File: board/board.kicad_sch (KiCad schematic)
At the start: 4 parts, among them J1 019_100BASE-T_with_CT, J2 009_1000BASE-T, J3 004_BASE-T_CT

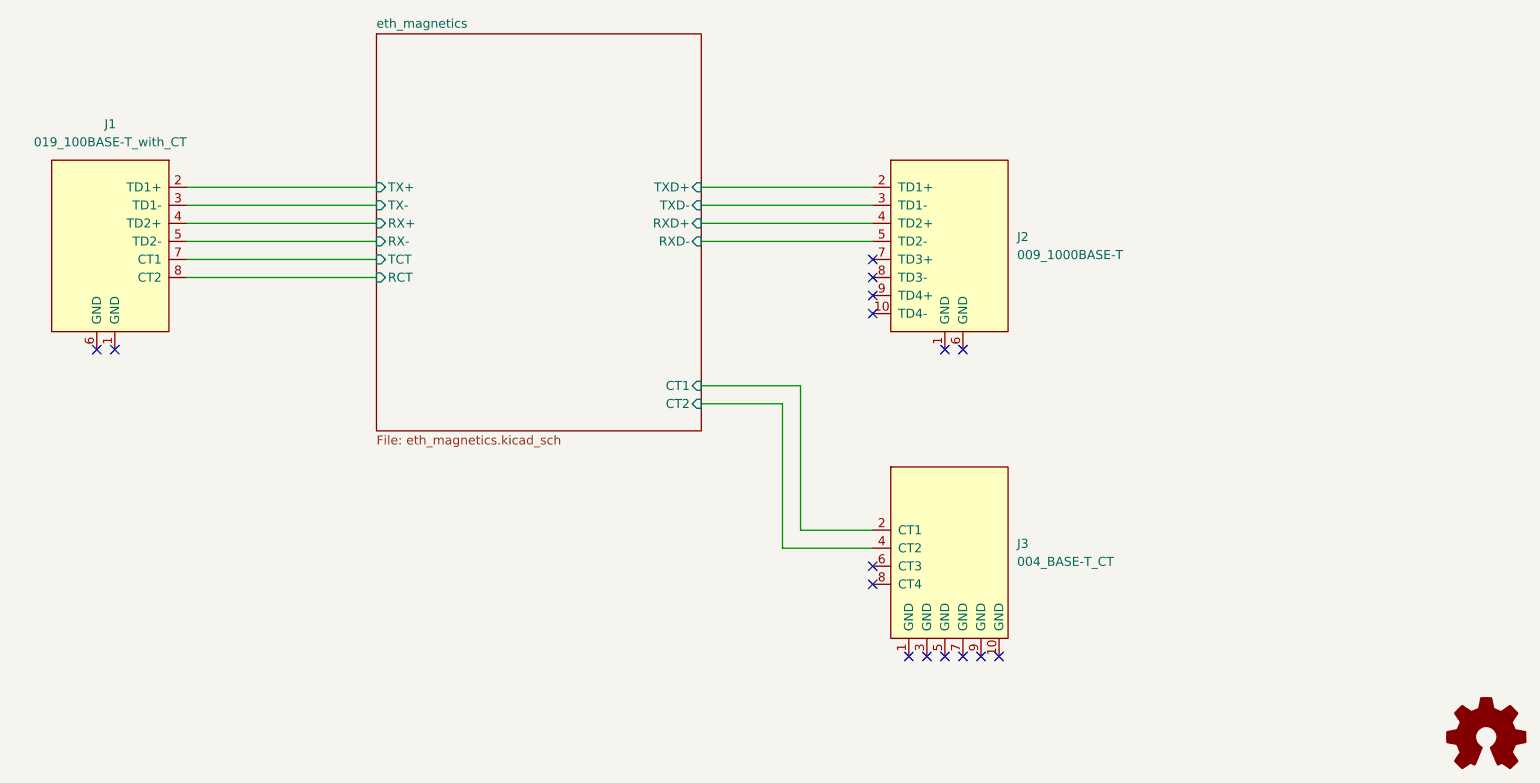
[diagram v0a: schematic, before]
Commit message: updated to use put_on_edge v1.0 connectors
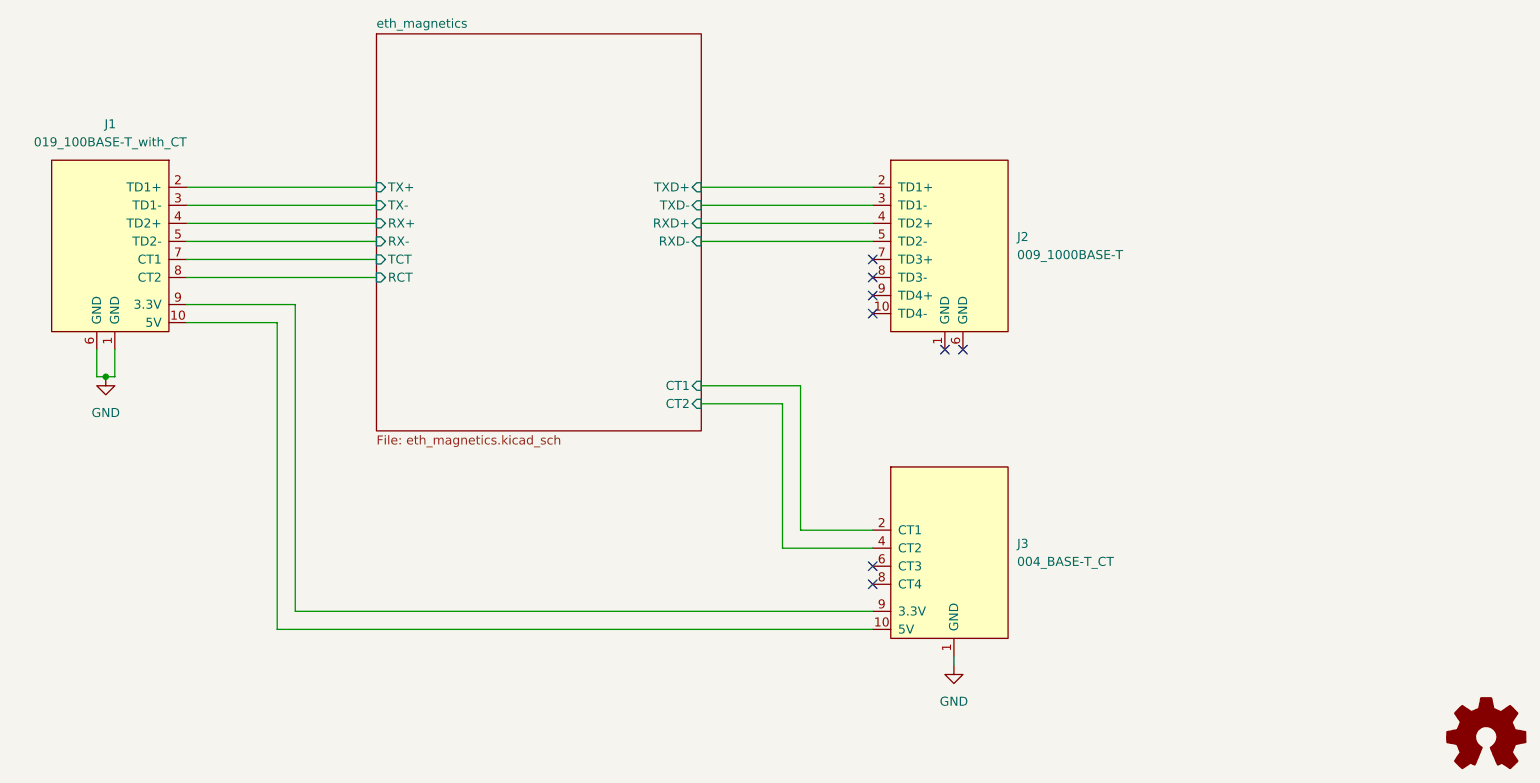
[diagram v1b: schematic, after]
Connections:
- net GND: now reaches J3.1 (GND)
- net GND: now also J1.1 (GND), J1.6 (GND)
- net at J3.10 (5V): now also J1.10 (5V)
- net at J3.9 (3.3V): now also J1.9 (3.3V)
- no-connect marks 16 -> 8
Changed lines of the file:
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@@
 (kicad_sch (version 20211123) (generator eeschema)
   (paper "A4")
-  (no_connect (at 80.01 102.87))
-  (no_connect (at 77.47 102.87))
+  (junction (at 78.74 106.68) (diameter 0) (color 0 0 0 0)
+  )
   (no_connect (at 186.69 90.17))
   (no_connect (at 186.69 95.25))
   (no_connect (at 186.69 92.71))
   (no_connect (at 186.69 97.79))
-  (no_connect (at 204.47 146.05))
-  (no_connect (at 194.31 146.05))
-  (no_connect (at 196.85 146.05))
-  (no_connect (at 199.39 146.05))
-  (no_connect (at 201.93 146.05))
   (no_connect (at 199.39 102.87))
   (no_connect (at 196.85 102.87))
-  (no_connect (at 191.77 146.05))
   (no_connect (at 186.69 135.89))
   (no_connect (at 186.69 133.35))
@@
     (stroke (width 0) (type default) (color 0 0 0 0))
   )
+  (wire (pts (xy 186.69 139.7) (xy 105.41 139.7))
+    (stroke (width 0) (type default) (color 0 0 0 0))
+  )
+  (wire (pts (xy 80.01 106.68) (xy 80.01 102.87))
+    (stroke (width 0) (type default) (color 0 0 0 0))
+  )
   (wire (pts (xy 90.17 82.55) (xy 116.84 82.55))
     (stroke (width 0) (type default) (color 0 0 0 0))
   )
+  (wire (pts (xy 77.47 102.87) (xy 77.47 106.68))
+    (stroke (width 0) (type default) (color 0 0 0 0))
+  )
   (wire (pts (xy 162.56 85.09) (xy 186.69 85.09))
     (stroke (width 0) (type default) (color 0 0 0 0))
@@
     (stroke (width 0) (type default) (color 0 0 0 0))
   )
+  (wire (pts (xy 77.47 106.68) (xy 78.74 106.68))
+    (stroke (width 0) (type default) (color 0 0 0 0))
+  )
   (wire (pts (xy 162.56 107.95) (xy 176.53 107.95))
     (stroke (width 0) (type default) (color 0 0 0 0))
   )
+  (wire (pts (xy 78.74 106.68) (xy 80.01 106.68))
+    (stroke (width 0) (type default) (color 0 0 0 0))
+  )
+  (wire (pts (xy 105.41 139.7) (xy 105.41 96.52))
+    (stroke (width 0) (type default) (color 0 0 0 0))
+  )
   (wire (pts (xy 176.53 128.27) (xy 186.69 128.27))
     (stroke (width 0) (type default) (color 0 0 0 0))
@@
     (stroke (width 0) (type default) (color 0 0 0 0))
   )
+  (wire (pts (xy 198.12 146.05) (xy 198.12 147.32))
+    (stroke (width 0) (type default) (color 0 0 0 0))
+  )
+  (wire (pts (xy 105.41 96.52) (xy 90.17 96.52))
+    (stroke (width 0) (type default) (color 0 0 0 0))
+  )
   (wire (pts (xy 173.99 110.49) (xy 173.99 130.81))
     (stroke (width 0) (type default) (color 0 0 0 0))
@@
     (stroke (width 0) (type default) (color 0 0 0 0))
   )
+  (wire (pts (xy 102.87 99.06) (xy 102.87 142.24))
+    (stroke (width 0) (type default) (color 0 0 0 0))
+  )
   (wire (pts (xy 90.17 85.09) (xy 116.84 85.09))
     (stroke (width 0) (type default) (color 0 0 0 0))
@@
     (stroke (width 0) (type default) (color 0 0 0 0))
   )
+  (wire (pts (xy 90.17 99.06) (xy 102.87 99.06))
+    (stroke (width 0) (type default) (color 0 0 0 0))
+  )
+  (wire (pts (xy 102.87 142.24) (xy 186.69 142.24))
+    (stroke (width 0) (type default) (color 0 0 0 0))
+  )
+  (symbol (lib_id "power:GND") (at 198.12 147.32 0) (unit 1)
+    (in_bom yes) (on_board yes) (fields_autoplaced)
+    (property "Reference" "#PWR0102" (id 0) (at 198.12 153.67 0)
+      (effects (font (size 1.27 1.27)) hide)
+    )
+    (property "Value" "GND" (id 1) (at 198.12 152.4 0))
+    (property "Footprint" "" (id 2) (at 198.12 147.32 0)
+      (effects (font (size 1.27 1.27)) hide)
+    )
+    (property "Datasheet" "" (id 3) (at 198.12 147.32 0)
+      (effects (font (size 1.27 1.27)) hide)
+    )
+    (pin "1")
+  )
   (symbol (lib_id "Graphic:Logo_Open_Hardware_Small") (at 273.05 157.48 0) (unit 1)
     (in_bom yes) (on_board yes) (fields_autoplaced)
@@
     )
     (property "Datasheet" "" (id 3) (at 205.74 115.57 0)
+      (effects (font (size 1.27 1.27)) hide)
+    )
+    (pin "1")
+    (pin "10")
+    (pin "2")
+    (pin "4")
+    (pin "6")
+    (pin "8")
+    (pin "9")
+  )
+  (symbol (lib_id "put_on_edge:019_100BASE-T_with_CT") (at 78.74 88.9 0) (mirror y) (unit 1)
+    (in_bom yes) (on_board yes) (fields_autoplaced)
+    (property "Reference" "J1" (id 0) (at 79.375 71.12 0))
+    (property "Value" "019_100BASE-T_with_CT" (id 1) (at 79.375 73.66 0))
+    (property "Footprint" "on_edge:on_edge_2x05_device" (id 2) (at 71.12 72.39 0)
+      (effects (font (size 1.27 1.27)) hide)
+    )
+    (property "Datasheet" "" (id 3) (at 71.12 72.39 0)
       (effects (font (size 1.27 1.27)) hide)
     )
@@
     (pin "9")
   )
-  (symbol (lib_id "put_on_edge:019_100BASE-T_with_CT") (at 78.74 88.9 0) (mirror y) (unit 1)
-    (in_bom yes) (on_board yes) (fields_autoplaced)
-    (property "Reference" "J1" (id 0) (at 79.375 71.12 0))
-    (property "Value" "019_100BASE-T_with_CT" (id 1) (at 79.375 73.66 0))
-    (property "Footprint" "on_edge:on_edge_2x05_device" (id 2) (at 71.12 72.39 0)
-      (effects (font (size 1.27 1.27)) hide)
-    )
-    (property "Datasheet" "" (id 3) (at 71.12 72.39 0)
-      (effects (font (size 1.27 1.27)) hide)
-    )
-    (pin "1")
-    (pin "2")
-    (pin "3")
-    (pin "4")
-    (pin "5")
-    (pin "6")
-    (pin "7")
-    (pin "8")
-  )
   (symbol (lib_id "put_on_edge:009_1000BASE-T") (at 198.12 88.9 0) (unit 1)
     (in_bom yes) (on_board yes) (fields_autoplaced)
@@
     (pin "9")
   )
+  (symbol (lib_id "power:GND") (at 78.74 106.68 0) (unit 1)
+    (in_bom yes) (on_board yes) (fields_autoplaced)
+    (property "Reference" "#PWR0101" (id 0) (at 78.74 113.03 0)
+      (effects (font (size 1.27 1.27)) hide)
+    )
+    (property "Value" "GND" (id 1) (at 78.74 111.76 0))
+    (property "Footprint" "" (id 2) (at 78.74 106.68 0)
+      (effects (font (size 1.27 1.27)) hide)
+    )
+    (property "Datasheet" "" (id 3) (at 78.74 106.68 0)
+      (effects (font (size 1.27 1.27)) hide)
+    )
+    (pin "1")
+  )
   (sheet (at 116.84 58.42) (size 45.72 55.88) (fields_autoplaced)
     (stroke (width 0.1524) (type solid) (color 0 0 0 0))
@@
   )
   (symbol_instances
+    (path "/f5bcd75e-356a-4da8-a9fe-623fa0e6ef56"
+      (reference "#PWR0101") (unit 1) (value "GND") (footprint "")
+    )
+    (path "/8abf2288-b2ff-4824-bade-ea97b1002519"
+      (reference "#PWR0102") (unit 1) (value "GND") (footprint "")
+    )
     (path "/df2e3995-6ff2-4214-8b56-2b5f6b2926fa"
       (reference "J1") (unit 1) (value "019_100BASE-T_with_CT") (footprint "on_edge:on_edge_2x05_device")
